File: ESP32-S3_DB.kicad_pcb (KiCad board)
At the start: 2 copper layers, 123.5 x 56.5 mm, 158 parts, among them CN1 JST_Battery, J1 TYPE-C-31-M12_13, J10 U2RS485_TX, J11 CAN_TX, J12 CAN_RX, J14 Conn_01x06, J15 Conn_01x10, J16 Conn_01x08, J17 U2RS485_RX, J18 U2RS485_DE_~{RE}, J19 U2RS485_TX, J2 A - B, J20 U2RS485_RX, J21 U2U, J22 PROG_Default, J3 H - L, J4 TYPE-C-31-M12_13, J5 EXT_LOAD, J6 R4_TX, J7 R4_RX, J8 Micro_SD_Card_Det1, J9 Conn_01x06, SW1 RESET, SW2 BOOT, SW3 ON/OFF, U1 ESP32-S3FH4R2, U2 UMH3N, U3 IP5306, U4 CH340X, U5 LD1117DT33CTR, U6 SP3071EEN-L/TR, U7 ATA6561-GAQW-N, X1 32.768KHz, Y1 40MHz

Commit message: Instigated routing
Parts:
- moved R16 2.85 mm to (197.9, 125.8)
- moved R4 1.81 mm to (206.4, 111.3)
- moved H3 1.49 mm to (210.9, 138.4)
- moved R5 0.95 mm to (201.5, 106.3)
- moved C36 0.50 mm to (180.1, 129.1)
- moved L4 0.50 mm to (183.3, 129.0)
- moved R10 0.50 mm to (181.8, 128.7)
- moved C40 0.23 mm to (203.4, 103.9)
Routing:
- net /INPUT POWER/VIN: track 0.00 -> 44.1 mm
- net /5V: track 0.00 -> 23.5 mm
- net Net-(J1-D+-PadA6): track 0.00 -> 8.81 mm, vias 0 -> 2
- net /OTG_D-: track 0.00 -> 8.25 mm, vias 0 -> 2
- net Net-(J1-D--PadA7): track 0.00 -> 8.13 mm
- net /INPUT POWER/CC2: track 0.00 -> 7.62 mm
- net /OTG_D+: track 0.00 -> 7.11 mm
- net /D-: track 0.00 -> 5.98 mm
- net /EXTERNAL CONNECTORS/CC1: track 0.00 -> 5.18 mm
- net /EXTERNAL CONNECTORS/CC2: track 0.00 -> 4.29 mm
- net /INPUT POWER/CC1: track 0.00 -> 3.42 mm
- net /D+: track 0.00 -> 2.64 mm
- added copper zone on B.Cu, net GND
- added copper zone on F.Cu, net GND
- added copper zone on In1.Cu, net GND
- added copper zone on In2.Cu, net GND
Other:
- outline, holes or cut-outs redrawn
- copper layers 2 -> 4

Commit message: Started ESP routing
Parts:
- moved J11 14.5 mm to (146.9, 95.8), turned to 0 degrees
- moved J10 11.5 mm to (171.1, 113.7), turned to 90 degrees
- moved R22 10.5 mm to (166.7, 106.8)
- moved J22 9.57 mm to (186.1, 107.6), turned to -90 degrees
- moved D13 6.82 mm to (182.7, 115.8)
- moved R3 6.78 mm to (124.2, 108.2)
- moved D3 6.16 mm to (170.4, 119.1), turned to 90 degrees
- moved R17 5.87 mm to (102.9, 119.9)
- moved R20 4.94 mm to (189.2, 110.4)
- moved D9 4.72 mm to (176.4, 119.1), turned to -90 degrees
- moved J17 4.27 mm to (171.1, 110.5), turned to 90 degrees
- moved D7 4.07 mm to (172.4, 119.1), turned to -90 degrees
- moved D12 4.05 mm to (182.7, 110.5)
- moved C19 3.81 mm to (191.7, 116.2)
- moved R43 3.75 mm to (185.4, 114.5), turned to 90 degrees
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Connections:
- net /CAN_H renamed /CAN_P
- net /CAN_L renamed /CAN_N
- net /RS_485/RS485_A renamed /RS_485/RS_485_P
- net /RS_485/RS485_B renamed /RS_485/RS_485_N
- net /RS_485_A renamed /RS485_P
- net /RS_485_B renamed /RS485_N
- J15 pad 3: /GPIO15 -> unconnected-(J15-Pin_3-Pad3)
- J15 pad 4: /GPIO16 -> unconnected-(J15-Pin_4-Pad4)
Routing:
- net /GPIO21: track 0.00 -> 73.1 mm, vias 0 -> 1
- net /GPIO33: track 0.00 -> 67.4 mm, vias 0 -> 1
- net /GPIO34: track 0.00 -> 64.2 mm, vias 0 -> 1
- net /GPIO35: track 0.00 -> 61.1 mm, vias 0 -> 1
- net /GPIO36: track 0.00 -> 58.4 mm, vias 0 -> 1
- net /GPIO37: track 0.00 -> 55.2 mm, vias 0 -> 1
- net /GPIO18: track 0.00 -> 47.9 mm, vias 0 -> 1
- net /GPIO17: track 0.00 -> 45.3 mm, vias 0 -> 1
- net /RS485_P: track 0.00 -> 26.0 mm
- net /CAN_P: track 0.00 -> 25.4 mm
- net /485_TRANS_TX: track 0.00 -> 24.5 mm
- net /CAN_N: track 0.00 -> 23.9 mm
- net /RS485_N: track 0.00 -> 23.0 mm
- net /V_BAT: track 0.00 -> 20.7 mm
- net Net-(U3-VIN): track 0.00 -> 16.9 mm
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- added copper zone on F.Cu, net Net-(U3-VOUT)
- added copper zone on F.Cu, net Net-(U5-VIN)
- added copper zone on F.Cu, net Net-(U5-VOUT)

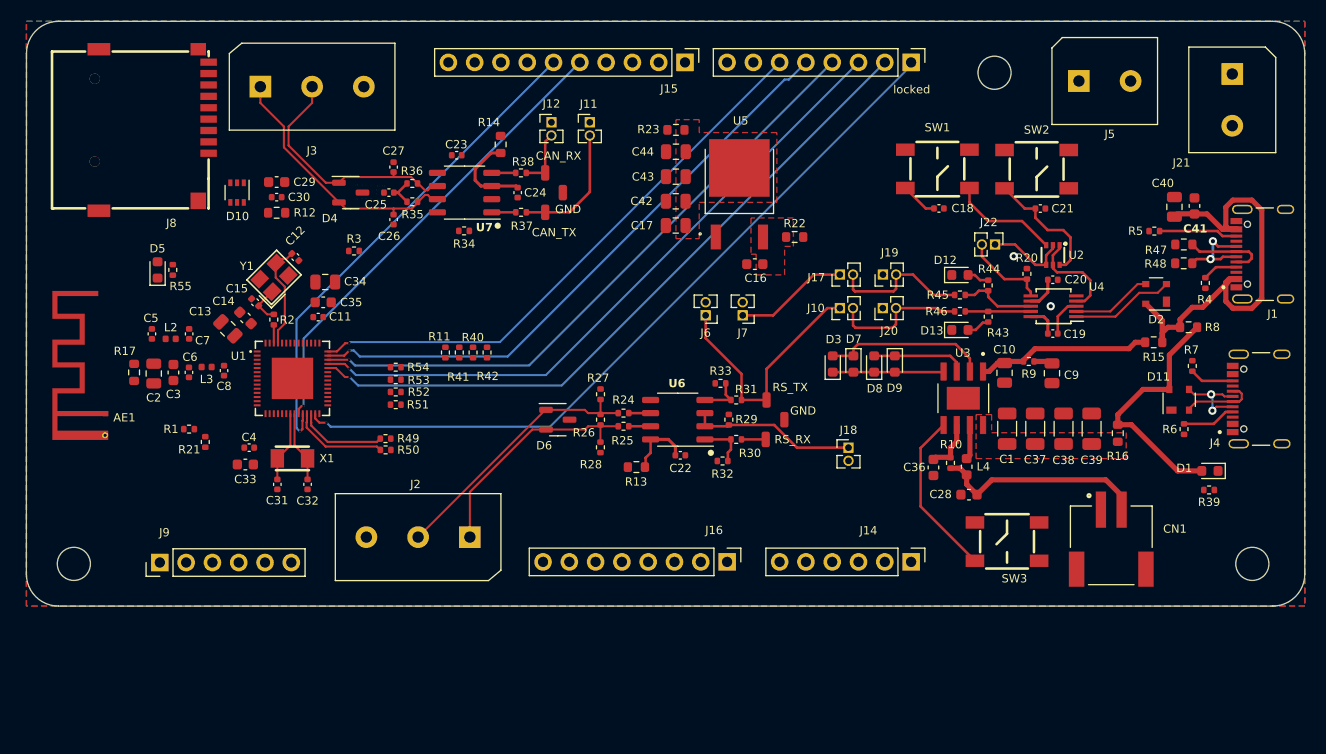
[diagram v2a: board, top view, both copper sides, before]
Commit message: Changed GPIO mapping
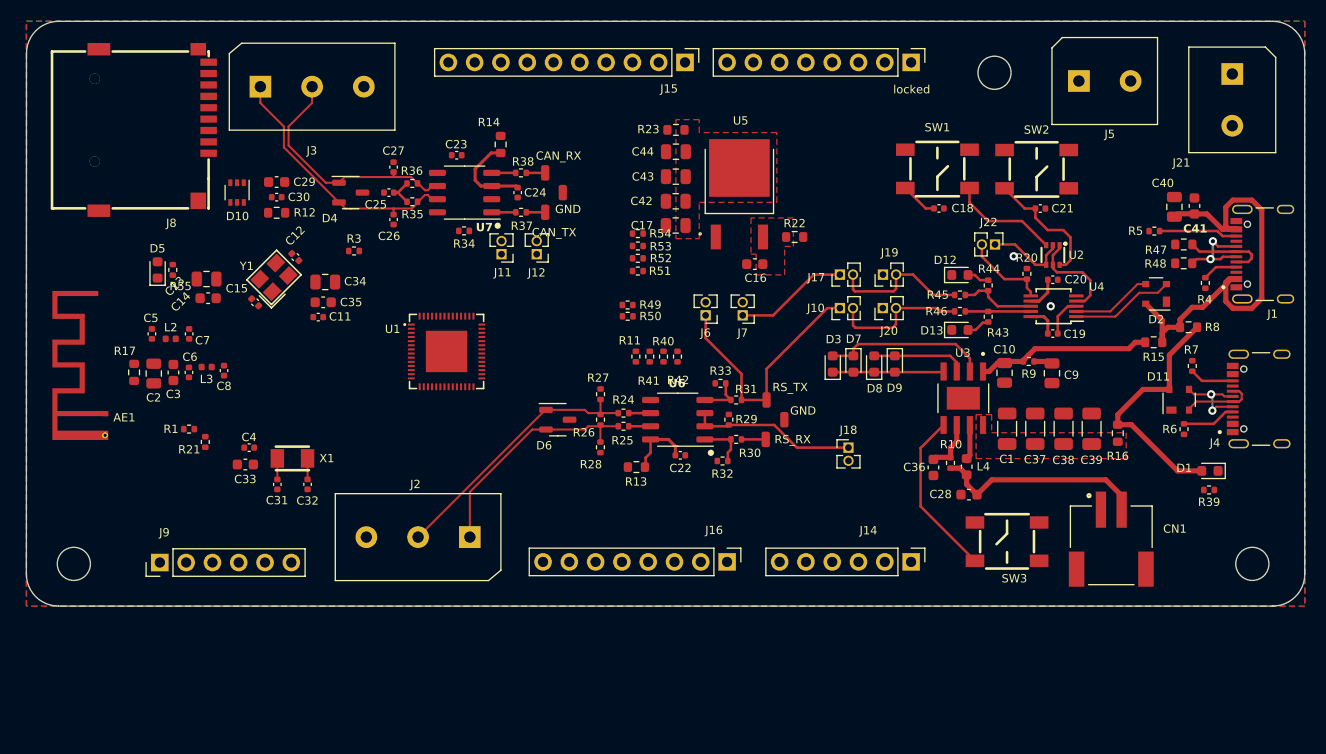
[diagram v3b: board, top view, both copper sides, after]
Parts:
- removed R2: 270, ESP32-S3_Dev_Board:R_0402_1005Metric
- moved R49 26.7 mm to (150.6, 113.4)
- moved R50 26.7 mm to (150.6, 114.5)
- moved R51 26.7 mm to (151.6, 110.1)
- moved R53 26.7 mm to (151.6, 107.7)
- moved R52 26.7 mm to (151.6, 108.9)
- moved R54 26.7 mm to (151.6, 106.5)
- moved R11 18.4 mm to (151.4, 118.4)
- moved R40 18.4 mm to (154.1, 118.4)
- moved R41 18.4 mm to (152.7, 118.4)
- moved R42 18.4 mm to (155.4, 118.4)
- moved J11 15.3 mm to (138.4, 108.5), turned to 180 degrees
- moved U1 15.1 mm to (133.1, 117.9)
- moved J12 12.8 mm to (141.8, 108.5), turned to 180 degrees
- moved C13 5.23 mm to (109.9, 110.9), turned to 180 degrees
- moved C14 4.08 mm to (110.1, 112.8), turned to 180 degrees
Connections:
- U1 pad 12: /CAN_TXD/GPIO7 -> unconnected-(U1-GPIO7-Pad12)
- U1 pad 13: /CAN_RXD/GPIO8 -> unconnected-(U1-GPIO8-Pad13)
- U1 pad 51: /RS-485_TX/GPIO45 -> /CAN_RXD/GPIO8
- U1 pad 52: /RS-485_RX/GPIO46 -> /CAN_TXD/GPIO7
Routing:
- net /GPIO21: track 73.1 -> 0.00 mm, vias 1 -> 0
- net /GPIO33: track 67.4 -> 0.00 mm, vias 1 -> 0
- net /GPIO34: track 64.2 -> 0.00 mm, vias 1 -> 0
- net /GPIO35: track 61.1 -> 0.00 mm, vias 1 -> 0
- net /GPIO36: track 58.4 -> 0.00 mm, vias 1 -> 0
- net /GPIO37: track 55.2 -> 0.00 mm, vias 1 -> 0
- net /GPIO18: track 47.9 -> 0.00 mm, vias 1 -> 0
- net /GPIO17: track 45.3 -> 0.00 mm, vias 1 -> 0
- net /CAN_TRANS_TXD: track 12.4 -> 1.82 mm
- net Net-(U1-XTAL_N): track 10.3 -> 0.00 mm
- net /ESP32-S3/D-: track 9.37 -> 0.00 mm
- net /ESP32-S3/D+: track 8.60 -> 0.00 mm
- net Net-(U1-XTAL_32K_P): track 6.87 -> 2.03 mm
- net Net-(U1-XTAL_32K_N): track 6.87 -> 2.03 mm
- net /CAN_TRANS_RXD: track 5.69 -> 1.83 mm
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
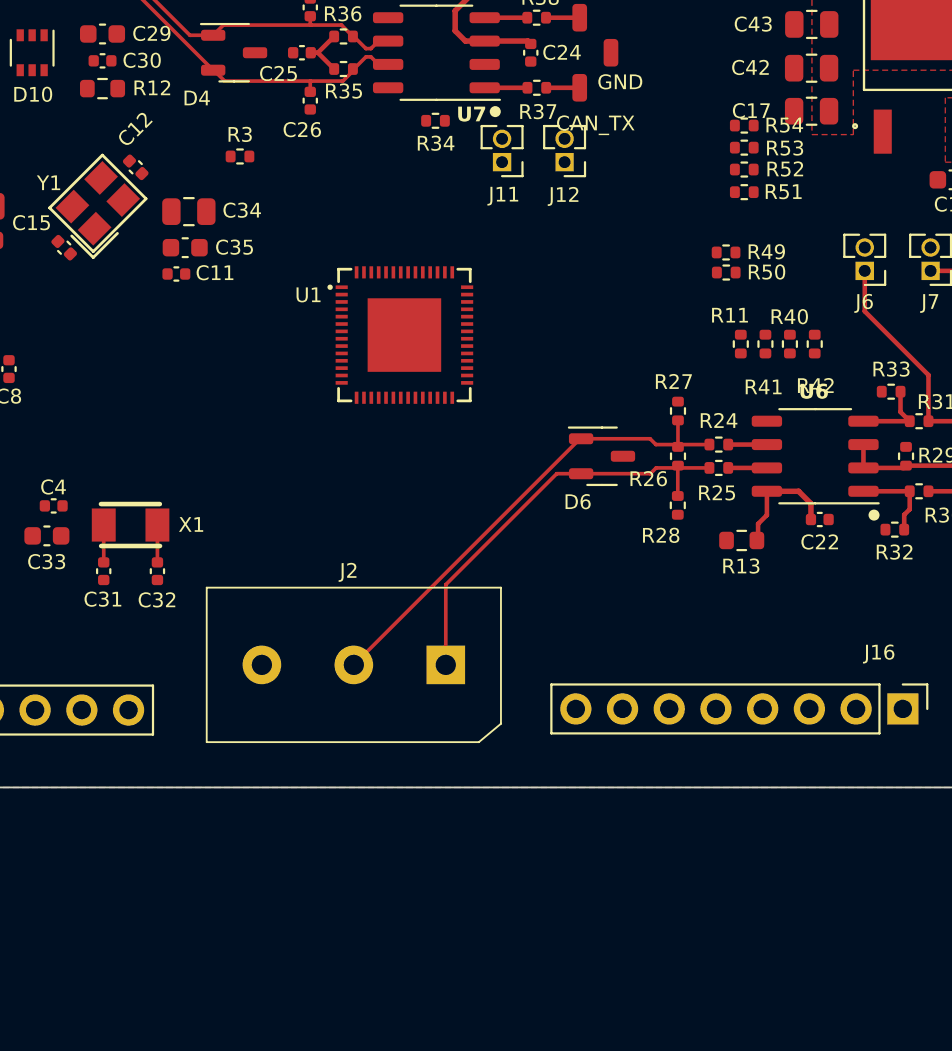
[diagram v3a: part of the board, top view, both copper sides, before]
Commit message: Changed MCU pin mapping
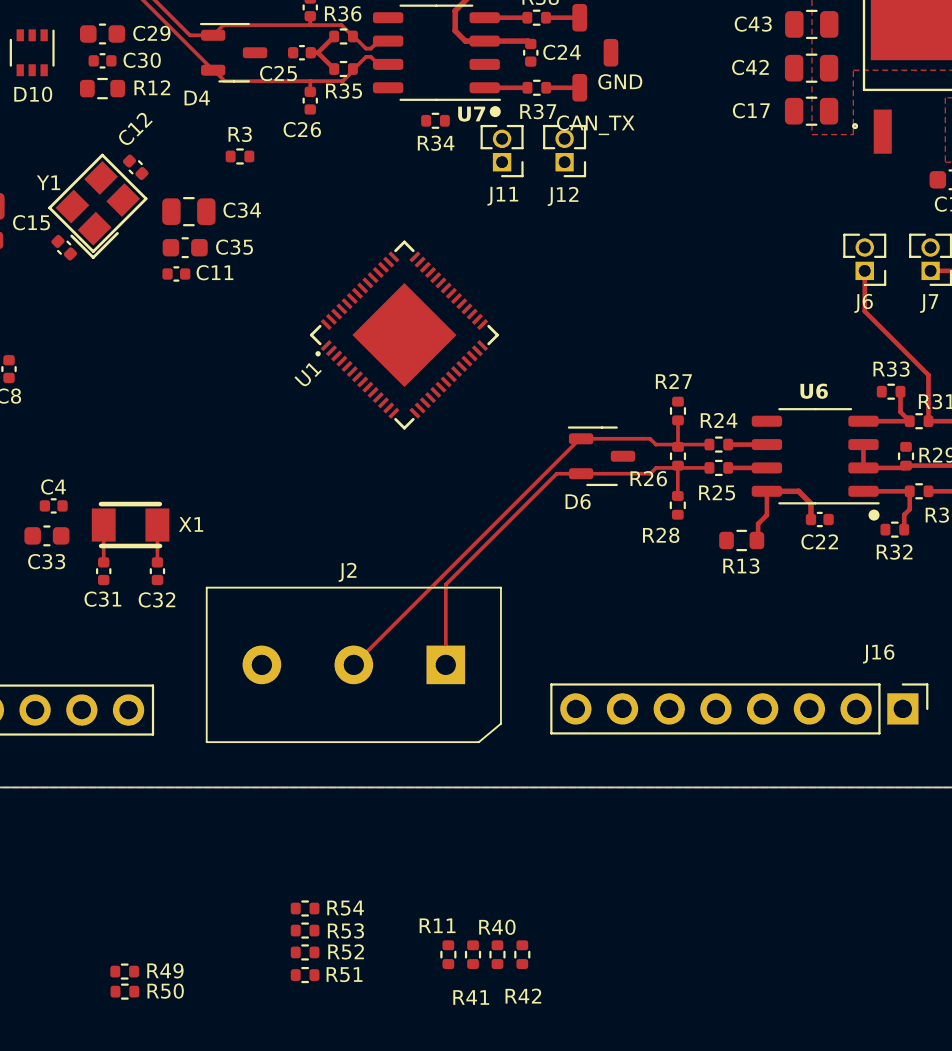
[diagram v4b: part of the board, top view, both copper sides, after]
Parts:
- moved R49 51.0 mm to (117.9, 152.5)
- moved R50 51.0 mm to (117.9, 153.6)
- moved R53 48.8 mm to (127.7, 150.3)
- moved R54 48.8 mm to (127.7, 149.1)
- moved R51 48.8 mm to (127.7, 152.7)
- moved R52 48.8 mm to (127.7, 151.5)
- moved R11 36.8 mm to (135.5, 151.6)
- moved R40 36.8 mm to (138.2, 151.6)
- moved R41 36.8 mm to (136.8, 151.6)
- moved R42 36.8 mm to (139.5, 151.6)
- turned U1 to 45 degrees
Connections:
- net /CAN_N renamed /CONN_CANL
- net /CAN_P renamed /CONN_CANH
- net /RS485_P renamed /CONN_RS485_A
- net /RS_485/RS_485_N renamed /RS_485/RS485_B
- net /RS_485/RS_485_P renamed /RS_485/RS485_A
- D6 pad 2: /RS485_N -> /RS_485/COMM_RS485_B
- J11 pad 1: /CAN_TXD/GPIO7 -> /CAN_TXD/GPIO36
- J12 pad 1: /CAN_RXD/GPIO8 -> /CAN_RXD/GPIO35
- J14 pad 1: /GPIO1 -> /GPIO11
- J14 pad 2: /GPIO2 -> /GPIO10
- J14 pad 3: /GPIO3 -> /GPIO9
- J14 pad 4: /GPIO4 -> /GPIO8
- J14 pad 5: /GPIO5 -> /GPIO7
- J15 pad 2: /GPIO14 -> /EXTERNAL CONNECTORS/GPIO14
- J15 pad 5: /GPIO17 -> /EXTERNAL CONNECTORS/GPIO17
- J18 pad 1: /R4_~{RE}_DE -> /RS485_~{RE}_DE/GPIO35
- J2 pad 1: /RS485_N -> /CONN_RS485_B
- J9 pad 1: /RS-485_TX/GPIO45 -> /3V3
- J9 pad 2: /RS-485_RX/GPIO46 -> /GPIO1
- J9 pad 3: /GPIO40 -> /GPIO2
- J9 pad 4: /GPIO41 -> /GPIO3
- J9 pad 5: /R4_~{RE}_DE -> /GPIO4
- J9 pad 6: /3V3 -> /GPIO5
- R25 pad 2: /RS485_N -> /RS_485/COMM_RS485_B
- R26 pad 1: /RS485_N -> /RS_485/COMM_RS485_B
- R28 pad 2: /RS485_N -> /RS_485/COMM_RS485_B
- R29 pad 2: /R4_~{RE}_DE -> /RS485_~{RE}_DE/GPIO35
- R51 pad 2: Net-(U1-GPIO10) -> unconnected-(R51-Pad2)
- R52 pad 2: Net-(U1-GPIO11) -> unconnected-(R52-Pad2)
- R53 pad 2: Net-(U1-GPIO12) -> unconnected-(R53-Pad2)
- R54 pad 2: Net-(U1-GPIO13) -> unconnected-(R54-Pad2)
- U1 pad 12: unconnected-(U1-GPIO7-Pad12) -> /GPIO7
- U1 pad 13: unconnected-(U1-GPIO8-Pad13) -> /GPIO8
- U1 pad 15: Net-(U1-GPIO10) -> /GPIO10
- U1 pad 16: Net-(U1-GPIO11) -> /GPIO11
- U1 pad 17: Net-(U1-GPIO12) -> /GPIO12
- U1 pad 18: Net-(U1-GPIO13) -> /GPIO13
- U1 pad 19: /GPIO14 -> /ESP32-S3/GPIO 14
- U1 pad 23: /GPIO17 -> /ESP32-S3/GPIO 17
- U1 pad 27: /GPIO21 -> /ESP32-S3/GPIO 21
- U1 pad 38: /GPIO33 -> /ESP32-S3/RS-485_TX/GPIO33
- U1 pad 39: /GPIO34 -> /ESP32-S3/RS-485_RX/GPIO34
- U1 pad 40: /GPIO35 -> /CAN_RXD/GPIO35
- U1 pad 41: /GPIO36 -> /RS485_~{RE}_DE/GPIO35
- U1 pad 42: /GPIO37 -> /CAN_TXD/GPIO36
- U1 pad 48: /R4_~{RE}_DE -> unconnected-(U1-MTMS-Pad48)
- U1 pad 51: /CAN_RXD/GPIO8 -> unconnected-(U1-GPIO45-Pad51)
- U1 pad 52: /CAN_TXD/GPIO7 -> unconnected-(U1-GPIO46-Pad52)
- U6 pad 2: /R4_~{RE}_DE -> /RS485_~{RE}_DE/GPIO35
- U6 pad 3: /R4_~{RE}_DE -> /RS485_~{RE}_DE/GPIO35
- locked pad 7: /CAN_RXD/GPIO8 -> /EXTERNAL CONNECTORS/CAN_RX/GPIO8
- locked pad 8: /CAN_TXD/GPIO7 -> /EXTERNAL CONNECTORS/CAN_TX/GPIO7
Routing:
- net /RS485_N: track 23.0 -> 0.00 mm
- net (no net): track 0.00 -> 23.0 mm
- net /RS485_~{RE}_DE/GPIO35: track 0.00 -> 16.1 mm
- net /R4_~{RE}_DE: track 16.1 -> 0.00 mm
